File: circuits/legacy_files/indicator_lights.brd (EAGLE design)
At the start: 10.1 x 14.9 mm, 6 parts, among them Q1 BSS84

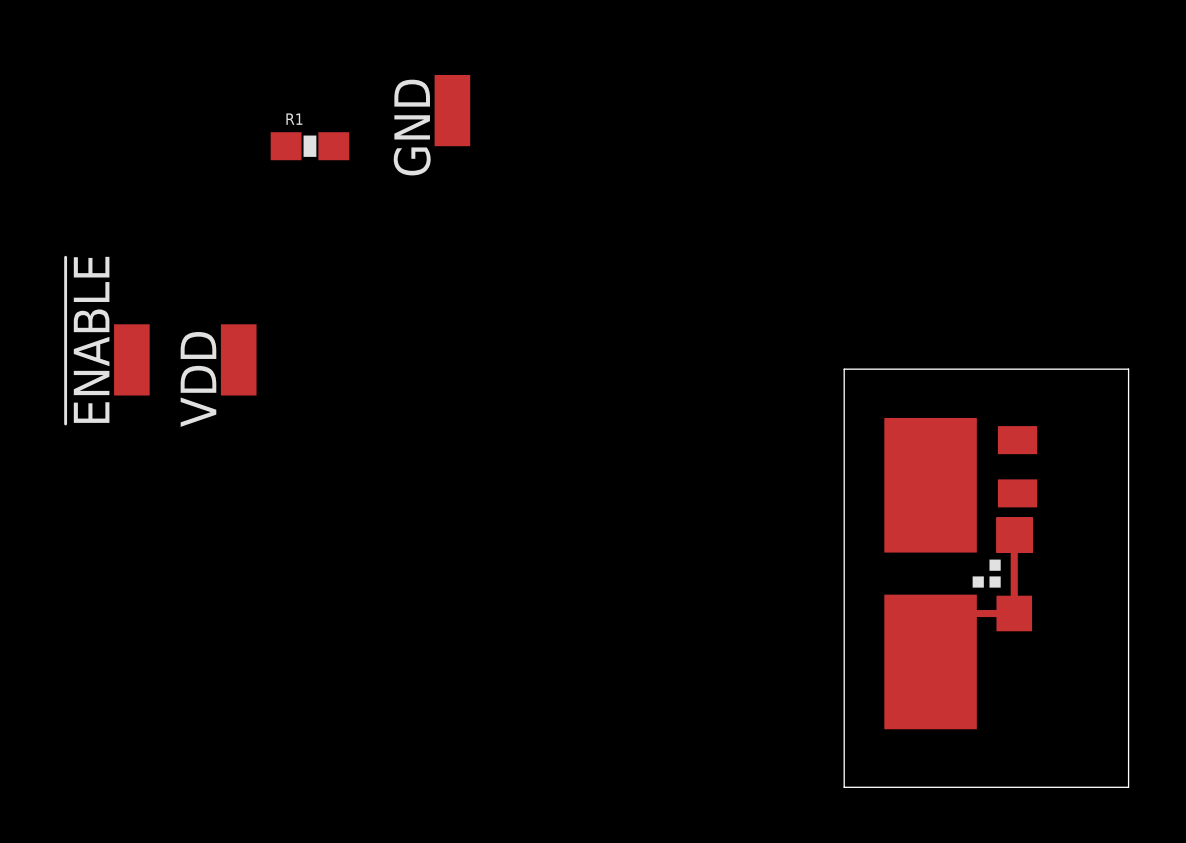
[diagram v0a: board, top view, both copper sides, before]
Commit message: Added new LED layout
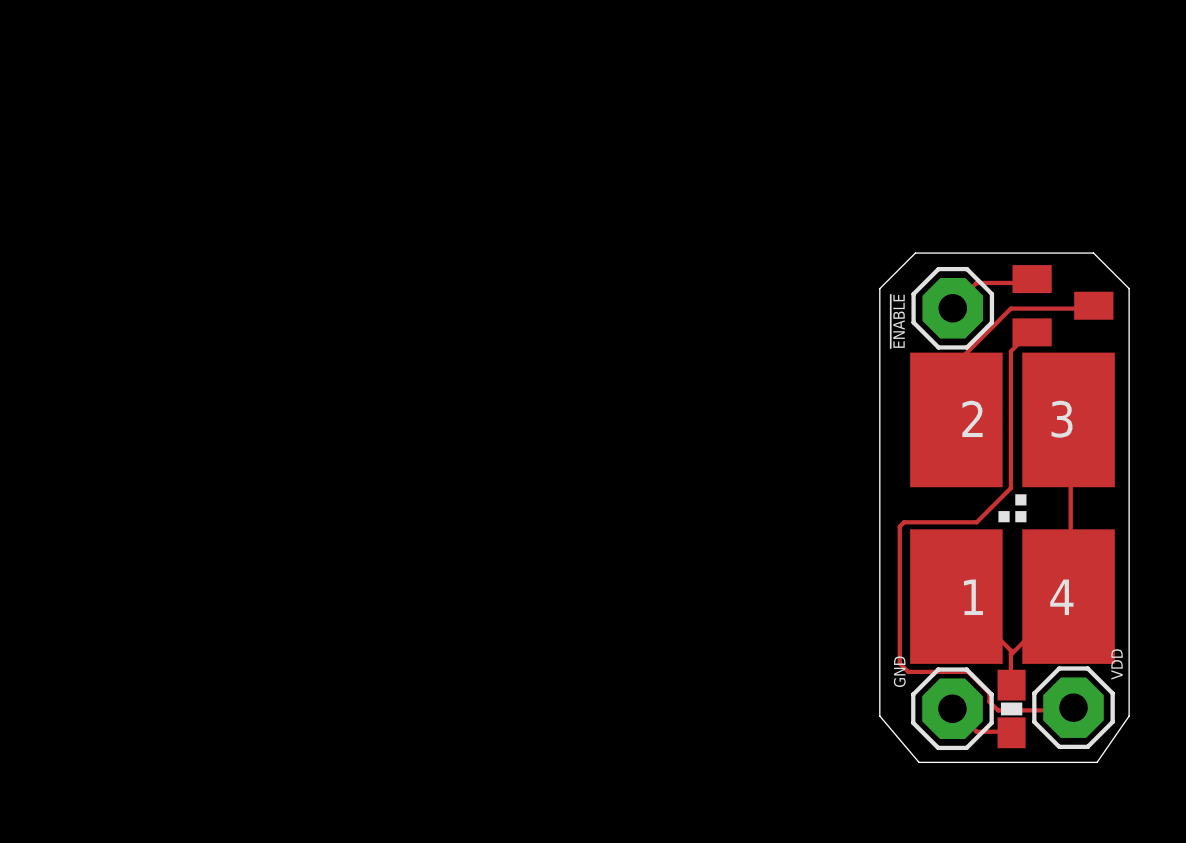
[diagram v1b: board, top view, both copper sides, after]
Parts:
- removed !ENABLE, GND, VDD: (no value), wirepad:SMD1,27-2,54
- added LSP1, LSP2, LSP3: MCS10B, solpad:MCS10B
- moved R1 32.1 mm to (5.97, 2.79), turned to 90 degrees
- moved Q1 6.35 mm to (7.80, 17.2), turned to 270 degrees
- moved LED1 2.51 mm to (6.00, 9.95)
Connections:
- net !ENABLE: now also LSP1.MP; no longer !ENABLE.1
- net GND: now also LSP3.MP; no longer GND.1
- net VDD: now also LSP2.MP; no longer VDD.1
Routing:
- net VDD: track 0.00 -> 22.4 mm
- net N$1: track 1.14 -> 7.85 mm
- net N$2: track 7.10 -> 13.3 mm
- net !ENABLE: track 0.00 -> 3.28 mm
- net GND: track 0.00 -> 2.46 mm
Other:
- board size 10.1 x 14.9 mm -> 8.9 x 18.2 mm
- board text added: "!ENABLE"
- board text added: "GND"
- board text added: "VDD"
